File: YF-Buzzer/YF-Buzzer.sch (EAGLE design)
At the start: 105 parts, among them IC1 74HC595N, IC2 74HC595N, IC3 74HC595N, IC4 74HC595N, IC5 74HC595N, IC6 74HC595N, IC7 74150N

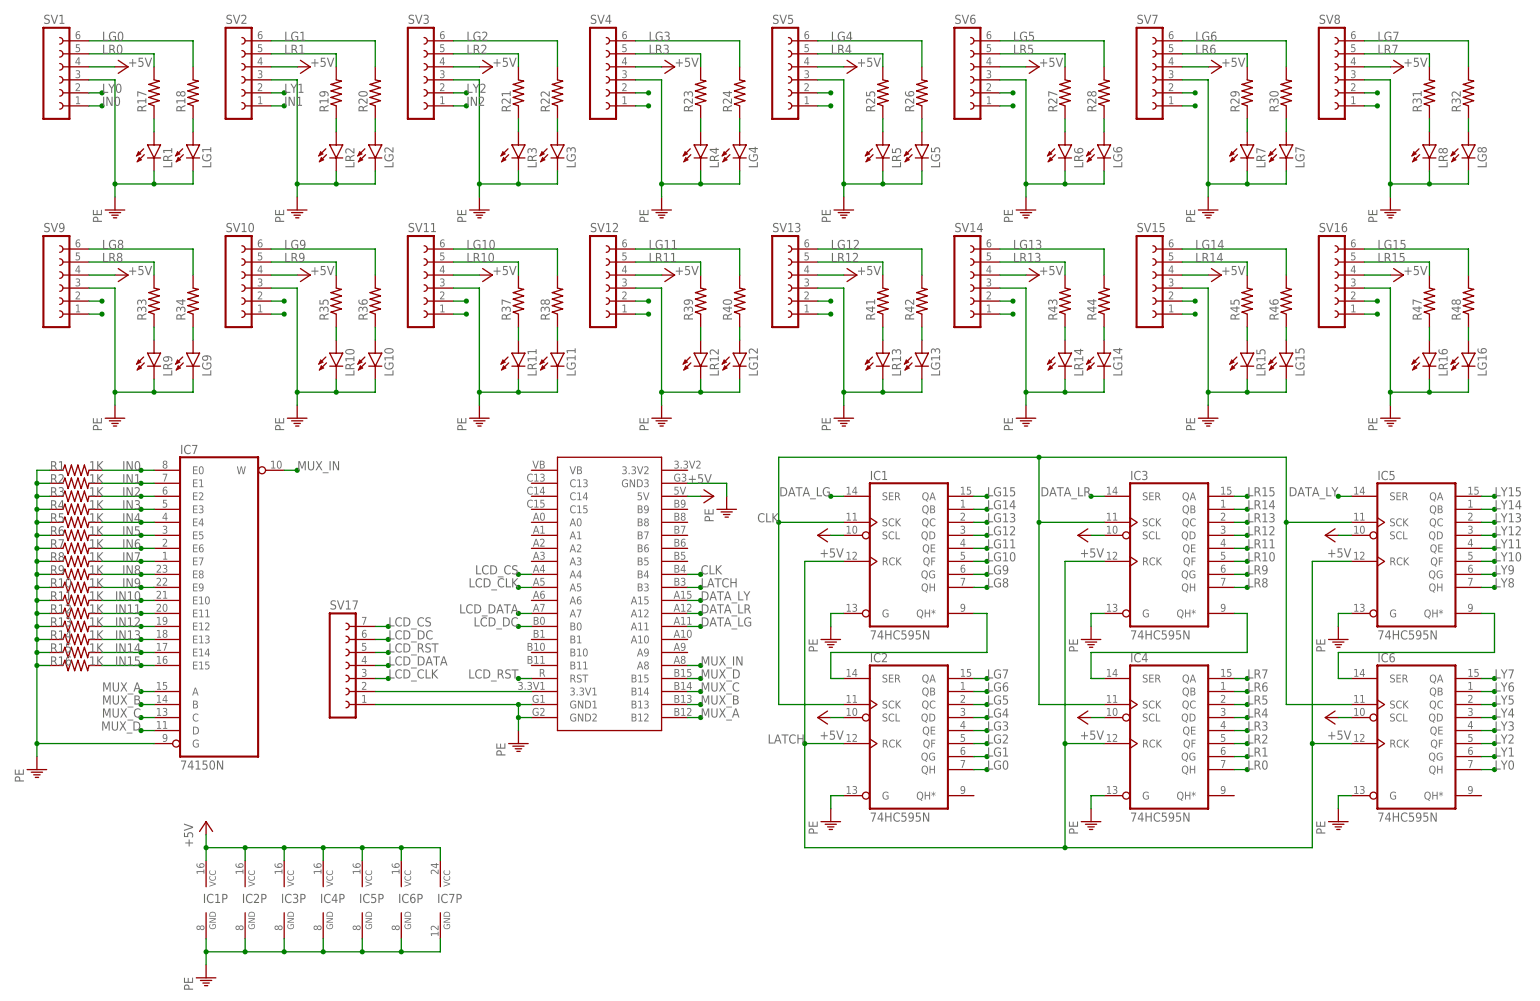
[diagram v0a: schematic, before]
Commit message: Removed LED's and cleaned up the circuit.
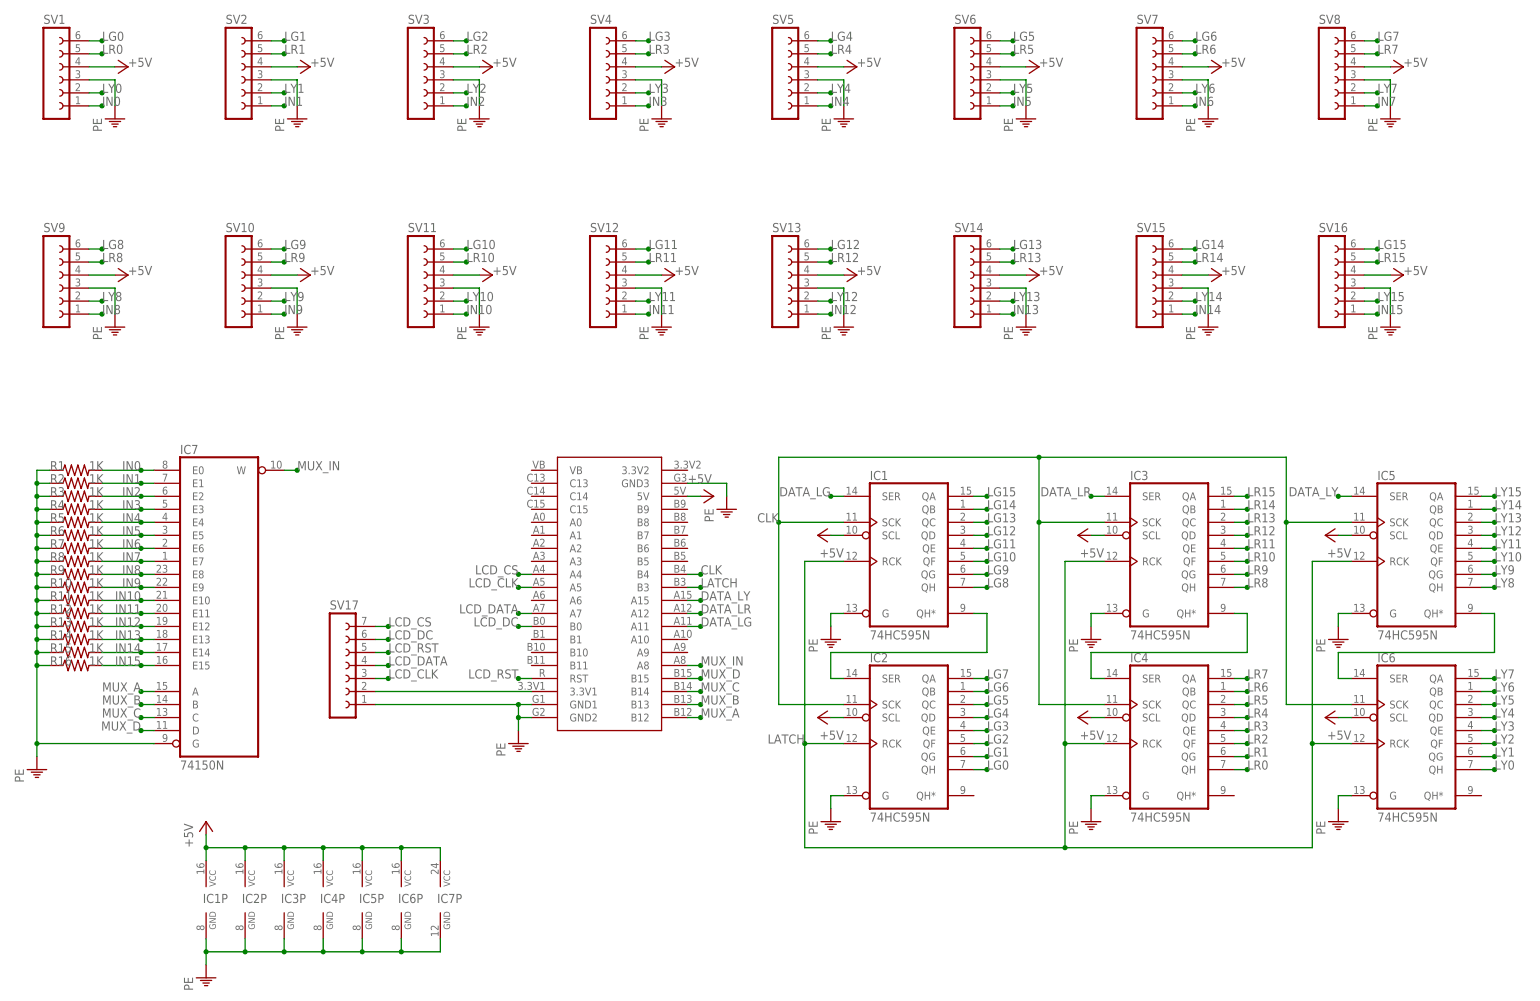
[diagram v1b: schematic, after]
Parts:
- removed LG1, LG10, LG11, LG12, LG13, LG14, LG15, LG16, LG2, LG3, LG4, LG5, LG6, LG7, LG8, LG9, LR1, LR10, LR11, LR12, LR13, LR14, LR15, LR16, LR2, LR3, LR4, LR5, LR6, LR7, LR8, LR9: (no value), led:LED3MM
- removed R17, R18, R19, R20, R21, R22, R23, R24, R25, R26, R27, R28, R29, R30, R31, R32, R33, R34, R35, R36, R37, R38, R39, R40, R41, R42, R43, R44, R45, R46, R47, R48: (no value), rcl:R-US_0207/10
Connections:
- removed net N$10: LG2.A, R20.1
- removed net N$101: LR14.A, R43.1
- removed net N$102: LG14.A, R44.1
- removed net N$105: SV14.2
- removed net N$106: SV14.1
- removed net N$113: LR15.A, R45.1
- removed net N$114: LG15.A, R46.1
- removed net N$117: SV15.2
- removed net N$118: SV15.1
- removed net N$125: LR16.A, R47.1
- removed net N$126: LG16.A, R48.1
- removed net N$129: SV16.2
- removed net N$130: SV16.1
- removed net N$137: LR1.A, R17.1
- removed net N$138: LG1.A, R18.1
- removed net N$15: LR3.A, R21.1
- removed net N$17: LG3.A, R22.1
- removed net N$22: LR5.A, R25.1
- removed net N$23: LG5.A, R26.1
- removed net N$26: SV5.2
- removed net N$27: SV5.1
- removed net N$28: LR4.A, R23.1
- removed net N$29: LG4.A, R24.1
- removed net N$32: SV4.2
- removed net N$33: SV4.1
- removed net N$34: LR6.A, R27.1
- removed net N$35: LG6.A, R28.1
- removed net N$39: SV6.2
- removed net N$40: SV6.1
- removed net N$41: LR7.A, R29.1
- removed net N$42: LG7.A, R30.1
- removed net N$45: SV7.2
- removed net N$46: SV7.1
- removed net N$47: LR8.A, R31.1
- removed net N$48: LG8.A, R32.1
- removed net N$51: SV8.2
- removed net N$52: SV8.1
- removed net N$53: LR9.A, R33.1
- removed net N$54: LG9.A, R34.1
- removed net N$57: SV9.2
- removed net N$58: SV9.1
- removed net N$59: LR11.A, R37.1
- removed net N$60: LG11.A, R38.1
- removed net N$63: SV11.2
- removed net N$64: SV11.1
- removed net N$71: LR12.A, R39.1
- removed net N$72: LG12.A, R40.1
- removed net N$73: LR10.A, R35.1
- removed net N$74: LG10.A, R36.1
- removed net N$77: SV10.2
- removed net N$78: SV10.1
- removed net N$81: SV12.2
- removed net N$82: SV12.1
- removed net N$89: LR13.A, R41.1
- removed net N$9: LR2.A, R19.1
- removed net N$90: LG13.A, R42.1
- removed net N$93: SV13.2
- removed net N$94: SV13.1
- net IN10: now also SV11.1
- net IN11: now also SV12.1
- net IN12: now also SV13.1
- net IN13: now also SV14.1
- net IN14: now also SV15.1
- net IN15: now also SV16.1
- net IN3: now also SV4.1
- net IN4: now also SV5.1
- net IN5: now also SV6.1
- net IN6: now also SV7.1
- net IN7: now also SV8.1
- net IN8: now also SV9.1
- net IN9: now also SV10.1
- net LG0: no longer R18.2
- net LG1: no longer R20.2
- net LG10: no longer R38.2
- net LG11: no longer R40.2
- net LG12: no longer R42.2
- net LG13: no longer R44.2
- net LG14: no longer R46.2
- net LG15: no longer R48.2
- net LG2: no longer R22.2
- net LG3: no longer R24.2
- net LG4: no longer R26.2
- net LG5: no longer R28.2
- net LG6: no longer R30.2
- net LG7: no longer R32.2
- net LG8: no longer R34.2
- net LG9: no longer R36.2
- net LR0: no longer R17.2
- net LR1: no longer R19.2
- net LR10: no longer R37.2
- net LR11: no longer R39.2
- net LR12: no longer R41.2
- net LR13: no longer R43.2
- net LR14: no longer R45.2
- net LR15: no longer R47.2
- net LR2: no longer R21.2
- net LR3: no longer R23.2
- net LR4: no longer R25.2
- net LR5: no longer R27.2
- net LR6: no longer R29.2
- net LR7: no longer R31.2
- net LR8: no longer R33.2
- net LR9: no longer R35.2
- net LY10: now also SV11.2
- net LY11: now also SV12.2
- net LY12: now also SV13.2
- net LY13: now also SV14.2
- net LY14: now also SV15.2
- net LY15: now also SV16.2
- net LY3: now also SV4.2
- net LY4: now also SV5.2
- net LY5: now also SV6.2
- net LY6: now also SV7.2
- net LY7: now also SV8.2
- net LY8: now also SV9.2
- net LY9: now also SV10.2
- net PE: no longer LG1.C, LG10.C, LG11.C, LG12.C, LG13.C, LG14.C, LG15.C, LG16.C, LG2.C, LG3.C, LG4.C, LG5.C, LG6.C, LG7.C, LG8.C, LG9.C, LR1.C, LR10.C, LR11.C, LR12.C, LR13.C, LR14.C, LR15.C, LR16.C, LR2.C, LR3.C, LR4.C, LR5.C, LR6.C, LR7.C, LR8.C, LR9.C
